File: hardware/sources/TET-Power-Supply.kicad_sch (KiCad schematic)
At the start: 27 parts, among them U10 TLV75533PDBVR, U5 5015, U6 5015, U7 5015, U8 INA226AQDGSRQ1, U9 TMP112AIDRLR

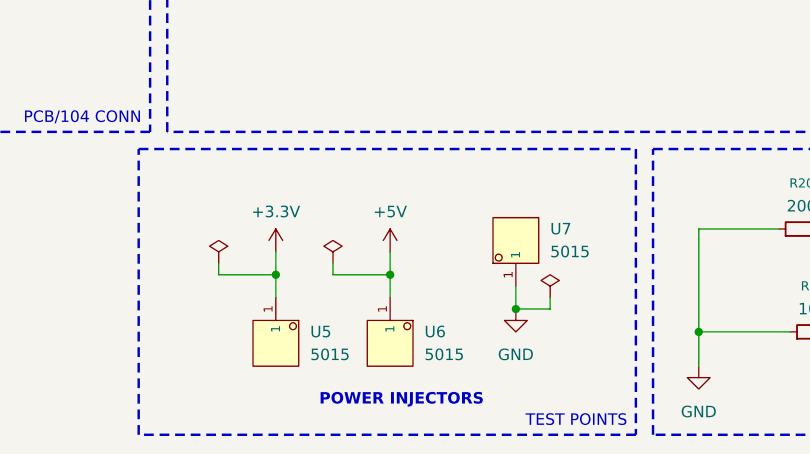
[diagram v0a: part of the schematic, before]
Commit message: hardware(schematics): remove 3.3 V power injector #2
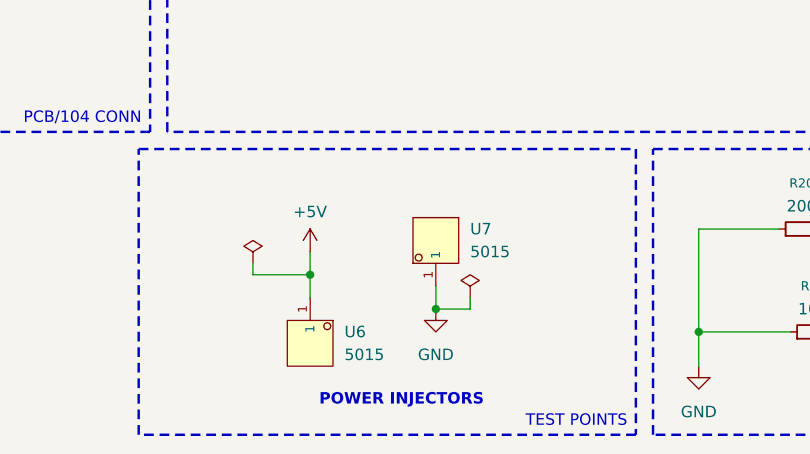
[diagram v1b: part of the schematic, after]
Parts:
- removed U5: 5015, TET-Footprints:TEST-SMD_L2.7-W1.0, symbol TET-Symbols:5015
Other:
- moved on the sheet: U6, U7

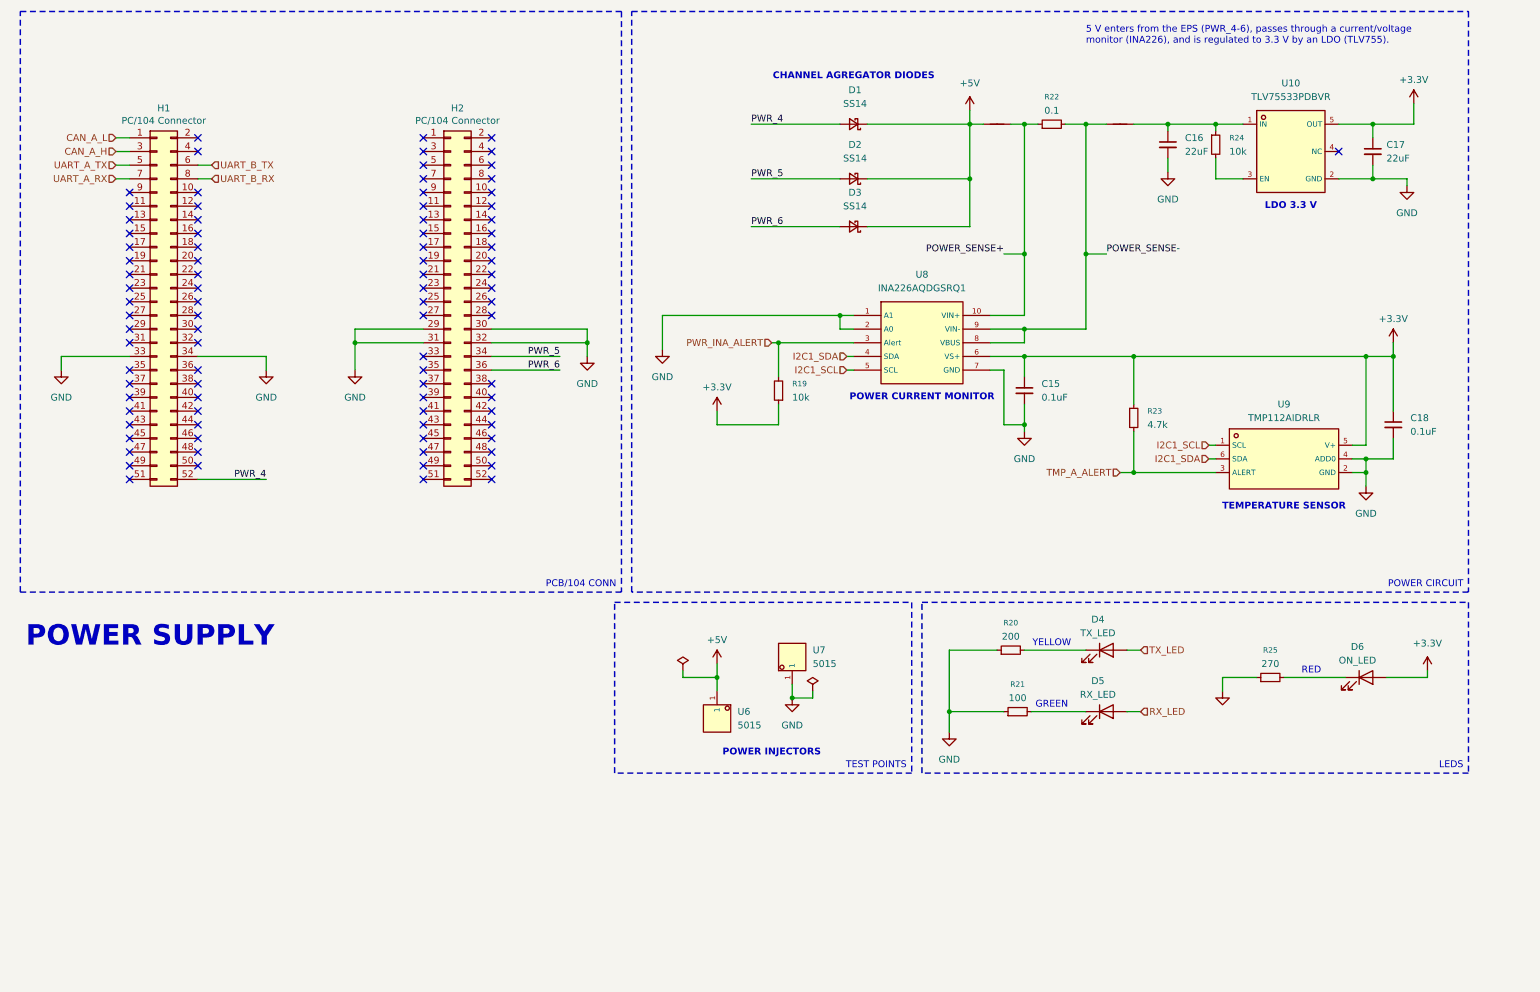
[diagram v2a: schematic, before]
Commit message: hardware(schematic): fix Electrical Rules Check (ERC)
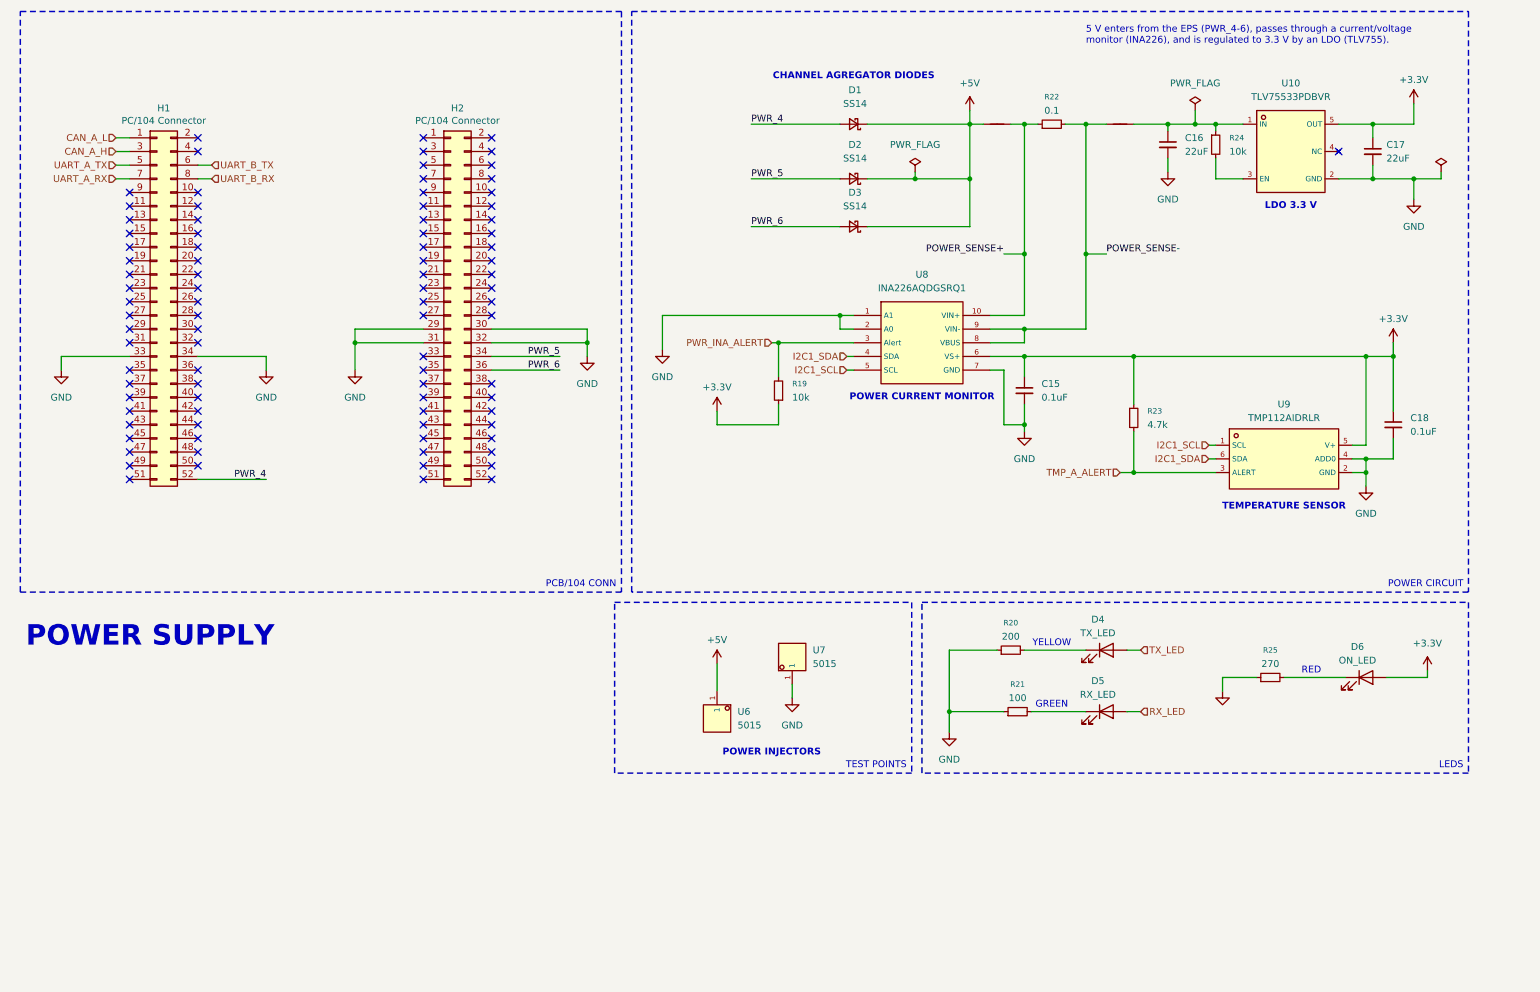
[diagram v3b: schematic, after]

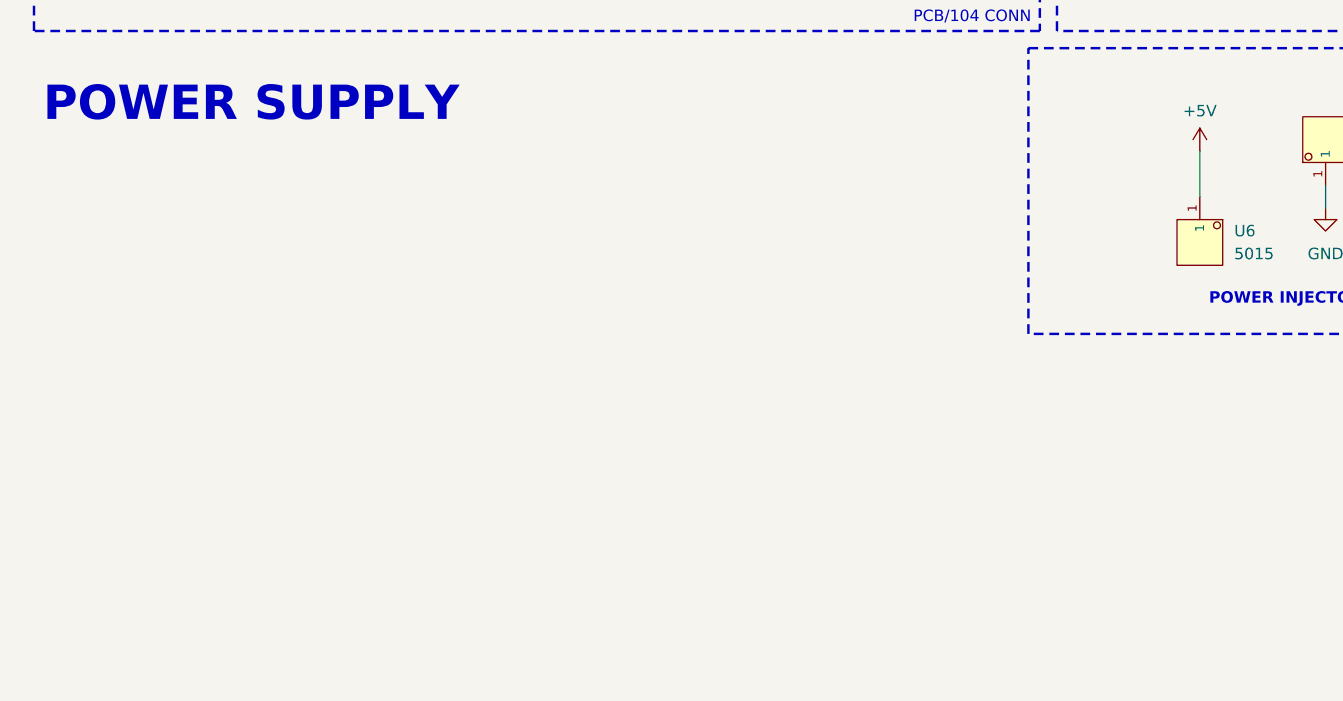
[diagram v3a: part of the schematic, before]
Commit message: hardware(schematic): update documentation for all sheets
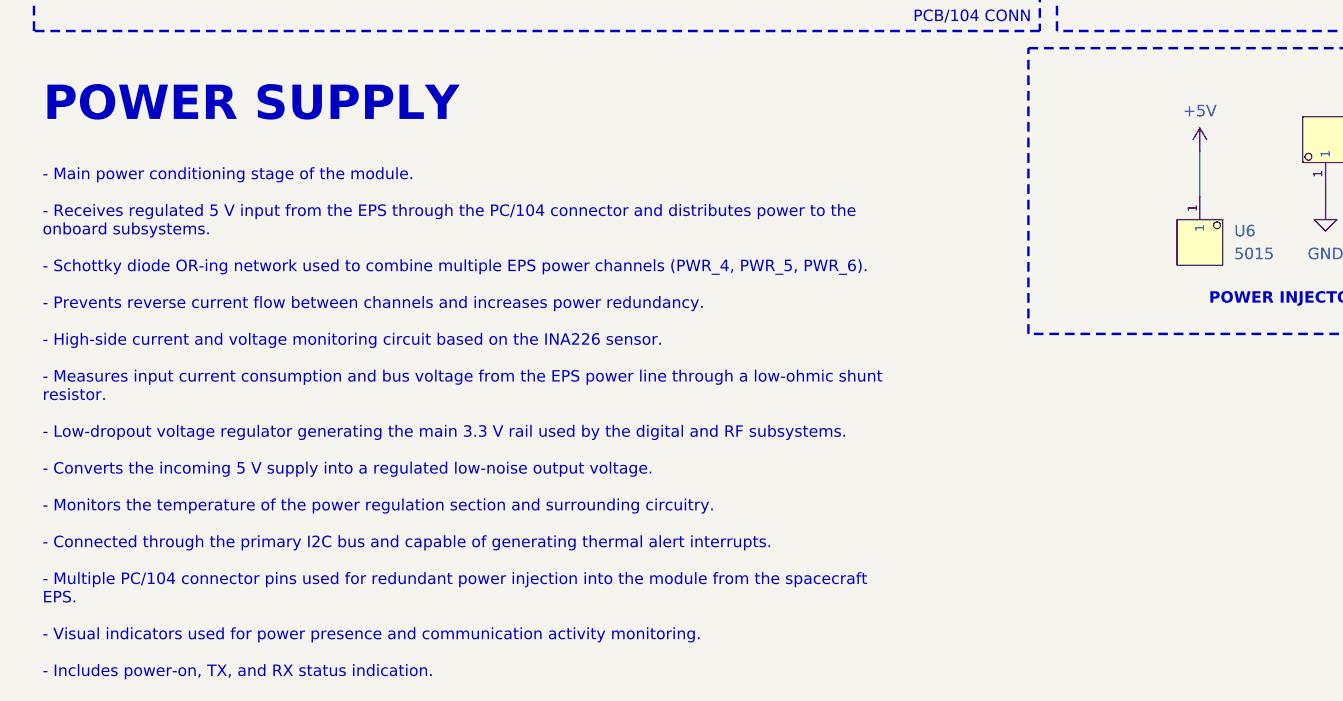
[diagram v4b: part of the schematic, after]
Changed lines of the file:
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@@
 		)
 	)
-	(text_box ""
+	(text_box "\n\n\n\n\n\n- Main power conditioning stage of the module.\n\n- Receives regulated 5 V input from the EPS through the PC/104 connector and distributes power to the onboard subsystems.\n\n- Schottky diode OR-ing network used to combine multiple EPS power channels (PWR_4, PWR_5, PWR_6).\n\n- Prevents reverse current flow between channels and increases power redundancy.\n\n- High-side current and voltage monitoring circuit based on the INA226 sensor.\n\n- Measures input current consumption and bus voltage from the EPS power line through a low-ohmic shunt resistor.\n\n- Low-dropout voltage regulator generating the main 3.3 V rail used by the digital and RF subsystems.\n\n- Converts the incoming 5 V supply into a regulated low-noise output voltage.\n\n- Monitors the temperature of the power regulation section and surrounding circuitry.\n\n- Connected through the primary I2C bus and capable of generating thermal alert interrupts.\n\n- Multiple PC/104 connector pins used for redundant power injection into the module from the spacecraft EPS.\n\n- Visual indicators used for power presence and communication activity monitoring.\n\n- Includes power-on, TX, and RX status indication."
 		(exclude_from_sim no)
 		(at 13.97 124.46 0)

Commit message: hardware(pcb_design): start PCB design
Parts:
- removed NT1, NT2: NetTie_2, symbol Device:NetTie_2
- H1, H2: footprint Connector_PinSocket_2.54mm:PinSocket_2x26_P2.54mm_Vertical -> TET-Footprints:PinHeader_2x26_P2.54mm_Vertical
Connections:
- net POWER_SENSE+ is gone; now on net +5V: R22.1, U8.10 (VIN+)
- net POWER_SENSE-: now also C16.1, R24.1, U10.1 (IN)
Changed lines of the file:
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@@
 	)
 	(junction
-		(at 200.66 59.69)
-		(diameter 0)
-		(color 0 0 0 0)
-	)
-	(junction
 		(at 232.41 35.56)
 		(diameter 0)
@@
 	(wire
 		(pts
-			(xy 200.66 35.56) (xy 200.66 59.69)
-		)
-		(stroke
-			(width 0)
-			(type default)
-		)
-	)
-	(wire
-		(pts
 			(xy 265.43 38.1) (xy 265.43 35.56)
 		)
@@
 	(wire
 		(pts
-			(xy 196.85 59.69) (xy 200.66 59.69)
-		)
-		(stroke
-			(width 0)
-			(type default)
-		)
-	)
-	(wire
-		(pts
 			(xy 59.69 78.74) (xy 59.69 81.28)
 		)
@@
 	(wire
 		(pts
-			(xy 212.09 35.56) (xy 215.9 35.56)
+			(xy 212.09 35.56) (xy 227.33 35.56)
 		)
 		(stroke
@@
 	(wire
 		(pts
-			(xy 200.66 59.69) (xy 200.66 71.12)
+			(xy 200.66 35.56) (xy 200.66 71.12)
 		)
 		(stroke
@@
 	(wire
 		(pts
-			(xy 198.12 35.56) (xy 200.66 35.56)
-		)
-		(stroke
-			(width 0)
-			(type default)
-		)
-	)
-	(wire
-		(pts
 			(xy 264.16 97.79) (xy 269.24 97.79)
 		)
@@
 	(wire
 		(pts
-			(xy 220.98 35.56) (xy 227.33 35.56)
-		)
-		(stroke
-			(width 0)
-			(type default)
-		)
-	)
-	(wire
-		(pts
 			(xy 46.99 78.74) (xy 59.69 78.74)
 		)
@@
 	(wire
 		(pts
-			(xy 190.5 35.56) (xy 193.04 35.56)
+			(xy 190.5 35.56) (xy 200.66 35.56)
 		)
 		(stroke
@@
 		)
 	)
-	(label "POWER_SENSE+"
-		(at 196.85 59.69 180)
-		(effects
-			(font
-				(size 1.27 1.27)
-			)
-			(justify right bottom)
-		)
-	)
 	(hierarchical_label "CAN_A_L"
 		(shape input)
@@
 	)
 	(symbol
-		(lib_id "Device:NetTie_2")
-		(at 195.58 35.56 0)
-		(unit 1)
-		(exclude_from_sim yes)
-		(in_bom no)
-		(on_board no)
-		(dnp no)
-		(fields_autoplaced yes)
-		(property "Reference" "NT1"
-			(at 195.58 30.48 0)
-			(effects
-				(font
-					(size 1.27 1.27)
-				)
-				(hide yes)
-			)
-		)
-		(property "Value" "NetTie_2"
-			(at 195.58 33.02 0)
-			(effects
-				(font
-					(size 1.27 1.27)
-				)
-				(hide yes)
-			)
-		)
-		(property "Footprint" ""
-			(at 195.58 35.56 0)
-			(effects
-				(font
-					(size 1.27 1.27)
-				)
-				(hide yes)
-			)
-		)
-		(property "Datasheet" "~"
-			(at 195.58 35.56 0)
-			(effects
-				(font
-					(size 1.27 1.27)
-				)
-				(hide yes)
-			)
-		)
-		(property "Description" "Net tie, 2 pins"
-			(at 195.58 35.56 0)
-			(effects
-				(font
-					(size 1.27 1.27)
-				)
-				(hide yes)
-			)
-		)
-		(pin "1"
-		)
-		(pin "2"
-		)
-		(instances
-			(project "TET"
-				(path "/9ad3bc3a-e567-4764-b6aa-630c8b7f3c7b/ea93ecaa-32da-4e78-85e1-01d04abbfc93"
-					(reference "NT1")
-					(unit 1)
-				)
-			)
-		)
-	)
-	(symbol
 		(lib_id "power:GND")
 		(at 264.16 102.87 0)
@@
 			)
 		)
-		(property "Footprint" "Connector_PinSocket_2.54mm:PinSocket_2x26_P2.54mm_Vertical"
+		(property "Footprint" "TET-Footprints:PinHeader_2x26_P2.54mm_Vertical"
 			(at 93.98 68.58 0)
 			(effects
@@
 	)
 	(symbol
-		(lib_id "Device:NetTie_2")
-		(at 218.44 35.56 0)
-		(unit 1)
-		(exclude_from_sim yes)
-		(in_bom no)
-		(on_board no)
-		(dnp no)
-		(fields_autoplaced yes)
-		(property "Reference" "NT2"
-			(at 218.44 30.48 0)
-			(effects
-				(font
-					(size 1.27 1.27)
-				)
-				(hide yes)
-			)
-		)
-		(property "Value" "NetTie_2"
-			(at 218.44 33.02 0)
-			(effects
-				(font
-					(size 1.27 1.27)
-				)
-				(hide yes)
-			)
-		)
-		(property "Footprint" ""
-			(at 218.44 35.56 0)
-			(effects
-				(font
-					(size 1.27 1.27)
-				)
-				(hide yes)
-			)
-		)
-		(property "Datasheet" "~"
-			(at 218.44 35.56 0)
-			(effects
-				(font
-					(size 1.27 1.27)
-				)
-				(hide yes)
-			)
-		)
-		(property "Description" "Net tie, 2 pins"
-			(at 218.44 35.56 0)
-			(effects
-				(font
-					(size 1.27 1.27)
-				)
-				(hide yes)
-			)
-		)
-		(pin "1"
-		)
-		(pin "2"
-		)
-		(instances
-			(project "TET"
-				(path "/9ad3bc3a-e567-4764-b6aa-630c8b7f3c7b/ea93ecaa-32da-4e78-85e1-01d04abbfc93"
-					(reference "NT2")
-					(unit 1)
-				)
-			)
-		)
-	)
-	(symbol
 		(lib_id "power:PWR_FLAG")
 		(at 278.13 44.45 0)
@@
 			)
 		)
-		(property "Footprint" "Connector_PinSocket_2.54mm:PinSocket_2x26_P2.54mm_Vertical"
+		(property "Footprint" "TET-Footprints:PinHeader_2x26_P2.54mm_Vertical"
 			(at 39.37 68.58 0)
 			(effects

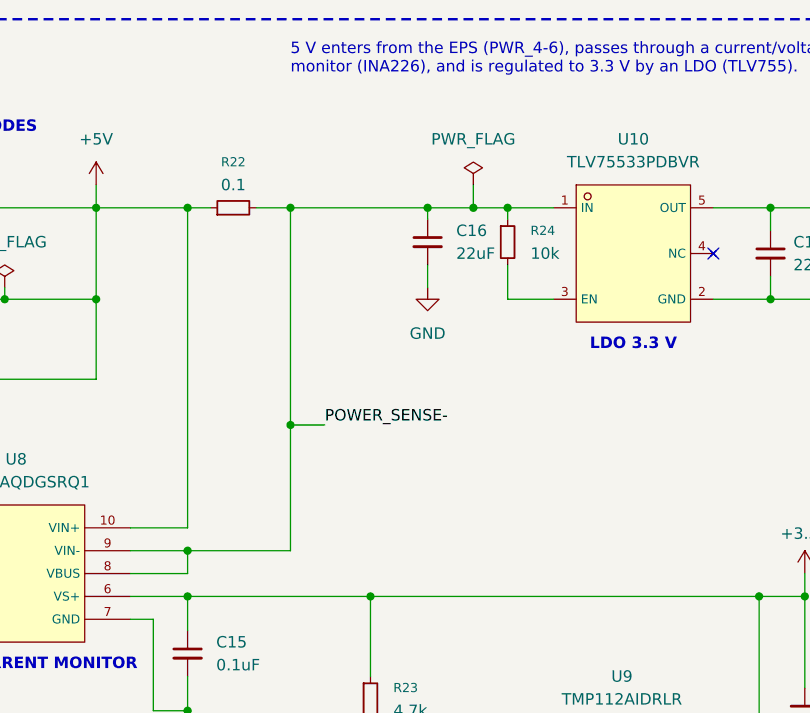
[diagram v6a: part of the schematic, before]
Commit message: hardware(pcb_design): components Micro-Placement
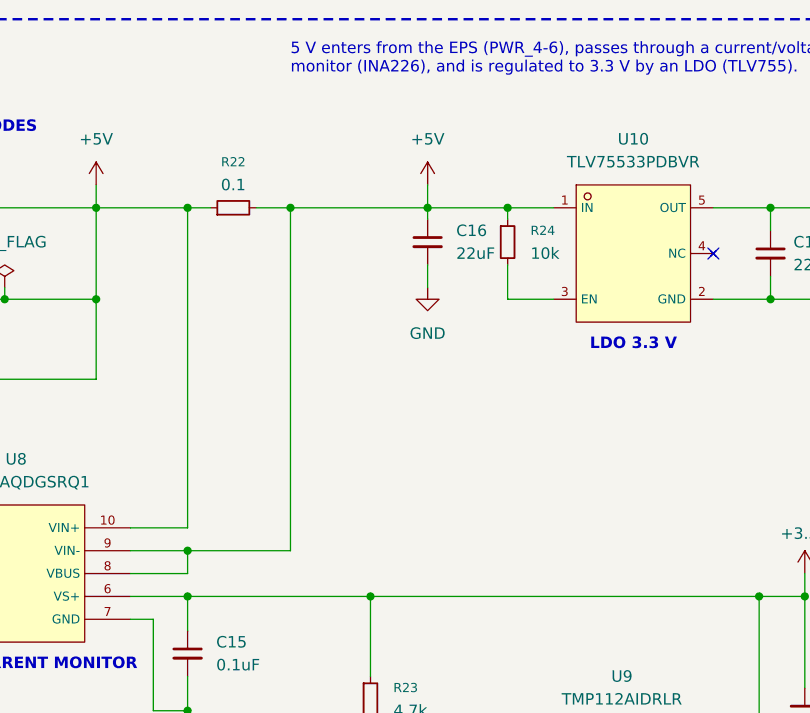
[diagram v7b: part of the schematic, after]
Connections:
- net POWER_SENSE- is gone; now on net +5V: C16.1, R22.2, R24.1, U10.1 (IN), U8.8 (VBUS), U8.9 (VIN-)
